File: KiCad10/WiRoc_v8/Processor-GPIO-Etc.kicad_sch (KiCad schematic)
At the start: 6 parts, among them U11 AllwinnerH3

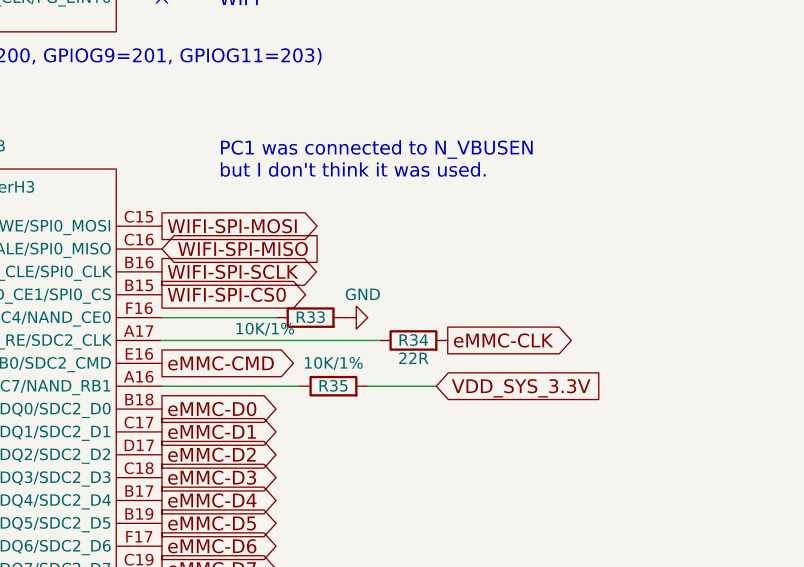
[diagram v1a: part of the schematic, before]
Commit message: add logo, improve layout
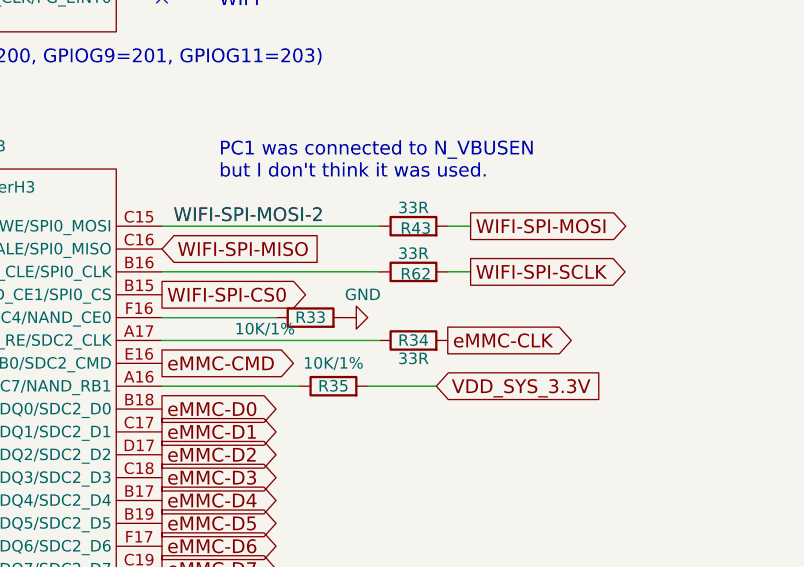
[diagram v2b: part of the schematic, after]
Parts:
- added R43, R62: 33R, Resistor_SMD:R_0402_1005Metric, symbol Device:R
- R34: value 22R -> 33R; LCSC Part # C25092 -> C25105; ManufacturerPartNumber 0402WGF220JTCE -> 0402WGF330JTCE
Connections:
- net WIFI-SPI-MOSI: now also R43.2; no longer U11.C15 (PC0/NAND_WE/SPI0_MOSI)
- net WIFI-SPI-SCLK: now also R62.2; no longer U11.B16 (PC2/NAND_CLE/SPI0_CLK)
- new net: R62.1, U11.B16 (PC2/NAND_CLE/SPI0_CLK)
- new net WIFI-SPI-MOSI-2: R43.1, U11.C15 (PC0/NAND_WE/SPI0_MOSI)
